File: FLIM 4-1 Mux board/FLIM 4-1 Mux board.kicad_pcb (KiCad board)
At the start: 4 copper layers, 74.5 x 100 mm, 59 parts, among them J2 RJ45_Shielded, J3 Conn_Coaxial, J4 Conn_Coaxial, J5 Conn_Coaxial, J6 Conn_Coaxial, J7 Conn_Coaxial, U1 ADM7150ARDZ-5.0, U2 74AHCT74D_118, U3 74AHCT74D_118, U4 SPDT RF switch, U5 SPDT RF switch, U6 SPDT RF switch

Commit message: Finished working draft of PCB - passes DRC
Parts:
- added J1: Barrel_Jack, Custom:CONN4_00165_TEN, F.Cu at (64.6, 41.7)
- moved J2 240.7 mm to (132.1, 50.9), turned to 90 degrees
- moved D4 218.6 mm to (117.0, 50.0)
- moved U3 213.5 mm to (108.0, 71.3)
- moved JP1 213.1 mm to (135.1, 62.6), turned to 90 degrees
- moved C18 209.0 mm to (133.3, 62.6), turned to -90 degrees
- moved C13 206.8 mm to (112.8, 67.0), turned to -90 degrees
- moved U2 206.3 mm to (92.0, 71.3)
- moved R1 199.0 mm to (95.7, 46.5)
- moved C9 197.8 mm to (103.6, 57.6), turned to -90 degrees
- moved C14 194.9 mm to (116.0, 56.4)
- moved C6 194.3 mm to (105.9, 46.0)
- moved C3 193.3 mm to (98.5, 47.5), turned to -90 degrees
- moved C15 192.8 mm to (113.9, 58.2), turned to -90 degrees
- moved C16 191.3 mm to (112.3, 58.2), turned to -90 degrees
- moved C12 190.5 mm to (96.8, 67.1), turned to -90 degrees
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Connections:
- D4 pad 1: /D1* -> /SH
- D4 pad 3: /SH -> /D1*
- D4 pad 4: /CLK* -> /D2*
- D4 pad 6: /D2* -> /CLK*
- RN1 pad 1: /CLK* -> /D1*
- RN1 pad 2: /D3* -> /D2*
- RN1 pad 3: /D2* -> /D3*
- RN1 pad 4: /D1* -> /CLK*
- RN1 pad 5: /D1 -> /CLK
- RN1 pad 6: /D2 -> /D3
- RN1 pad 7: /D3 -> /D2
- RN1 pad 8: /CLK -> /D1
- U2 pad 12: /D2 -> /D3
- U2 pad 2: /D1 -> /D2
- U2 pad 5: /A1 -> /A2
- U2 pad 6: /B1 -> /B2
- U2 pad 8: /B2 -> /B3
- U2 pad 9: /A2 -> /A3
- U3 pad 2: /D3 -> /D1
- U3 pad 5: /A3 -> /A1
- U3 pad 6: /B3 -> /B1
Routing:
- net GND: track 0.00 -> 309.3 mm, vias 0 -> 1602
- net +5VA: track 0.00 -> 85.4 mm, vias 0 -> 5
- net /CLK: track 0.00 -> 78.2 mm, vias 0 -> 8
- net /A2: track 0.00 -> 65.7 mm, vias 0 -> 2
- net /B3: track 0.00 -> 62.1 mm, vias 0 -> 2
- net /B2: track 0.00 -> 62.1 mm, vias 0 -> 2
- net /A3: track 0.00 -> 60.4 mm, vias 0 -> 2
- net /A1: track 0.00 -> 52.7 mm, vias 0 -> 2
- net /SH: track 0.00 -> 52.2 mm
- net /B1: track 0.00 -> 48.9 mm, vias 0 -> 2
- net /D2: track 0.00 -> 39.5 mm, vias 0 -> 3
- net /CLK*: track 0.00 -> 29.8 mm, vias 0 -> 4
- net /D1: track 0.00 -> 29.7 mm, vias 0 -> 3
- net /D3: track 0.00 -> 29.7 mm, vias 0 -> 3
- net /D3*: track 0.00 -> 26.3 mm, vias 0 -> 4
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- added copper zone on F.Cu, net +12VA
- added copper zone on F.Cu, net +5VA
- added copper zone on B.Cu, net GND
- added copper zone on In1.Cu, net GND
- added copper zone on In2.Cu, net GND
- added copper zone on F.Cu, net GNDPWR

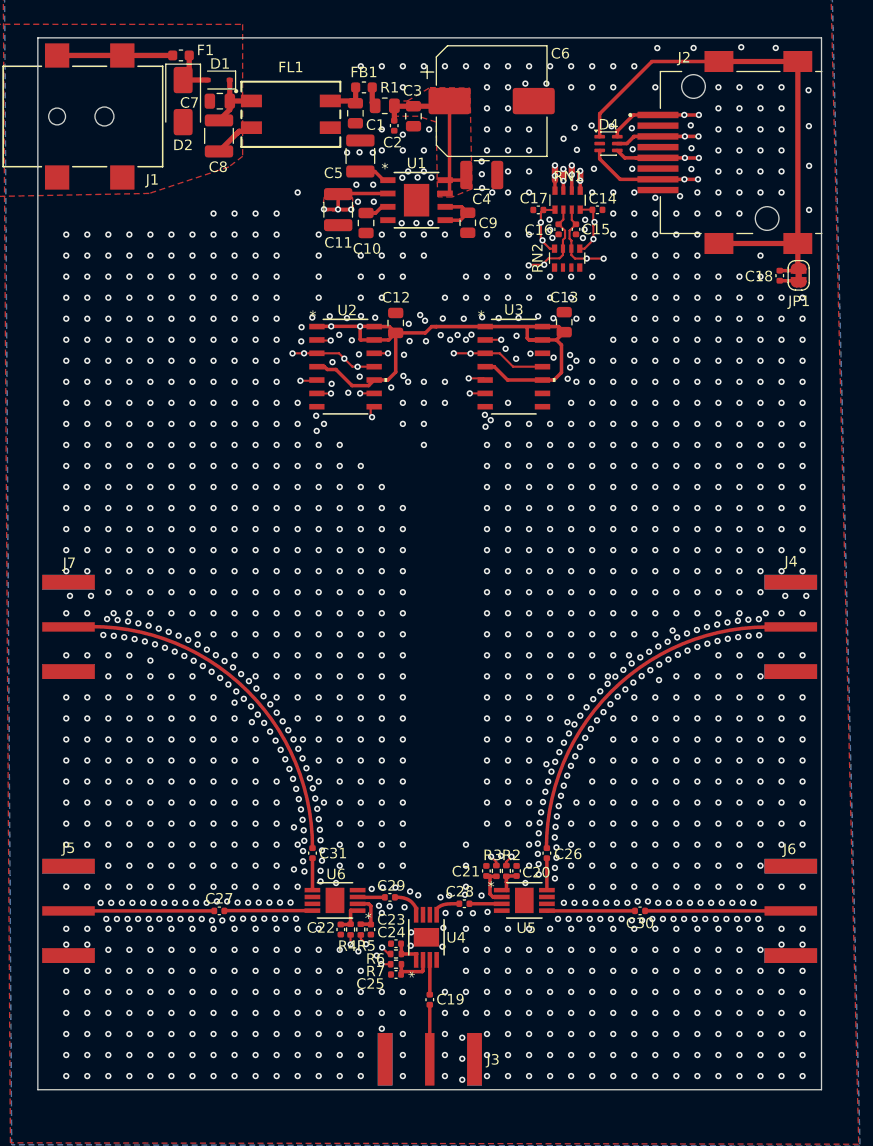
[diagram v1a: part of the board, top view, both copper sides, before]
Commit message: Backup copy of just guard vias, not ground stitching
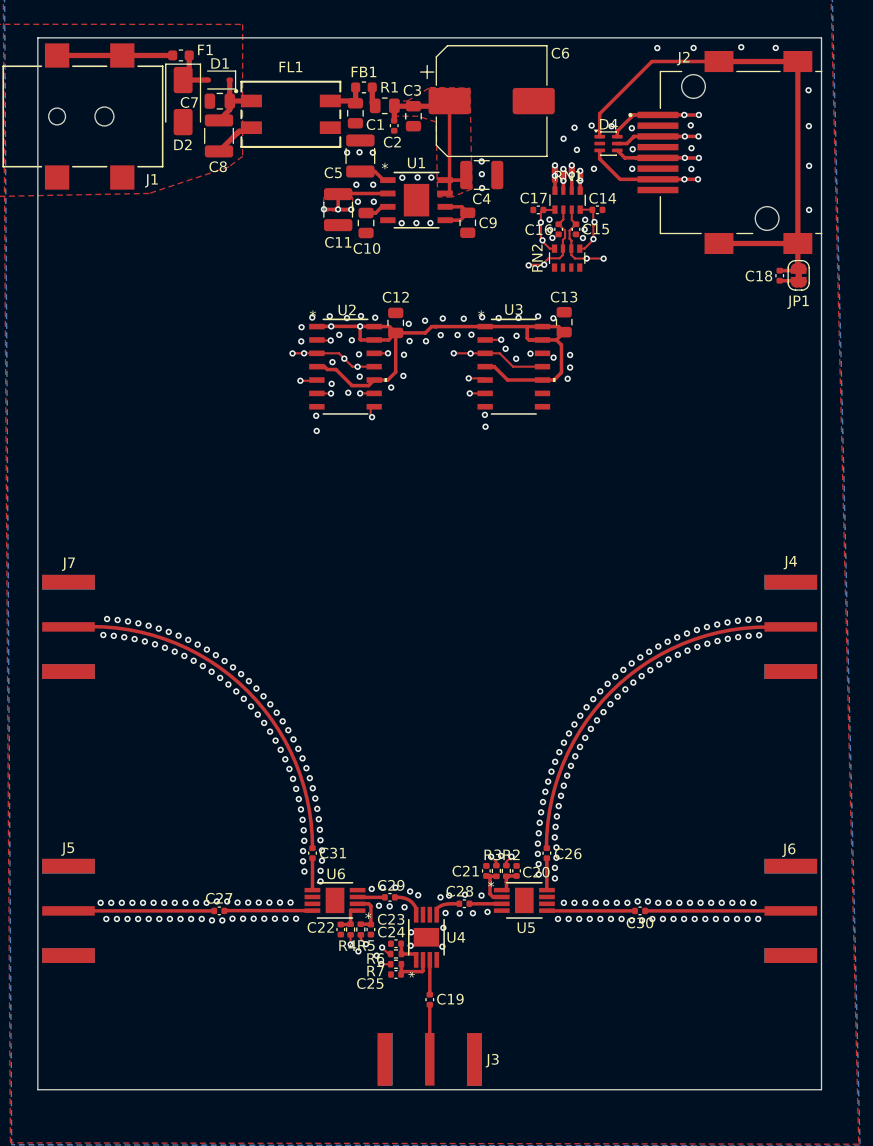
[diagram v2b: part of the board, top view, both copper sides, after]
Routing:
- net GND: vias 1602 -> 328

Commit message: Working draft with grnound stitching
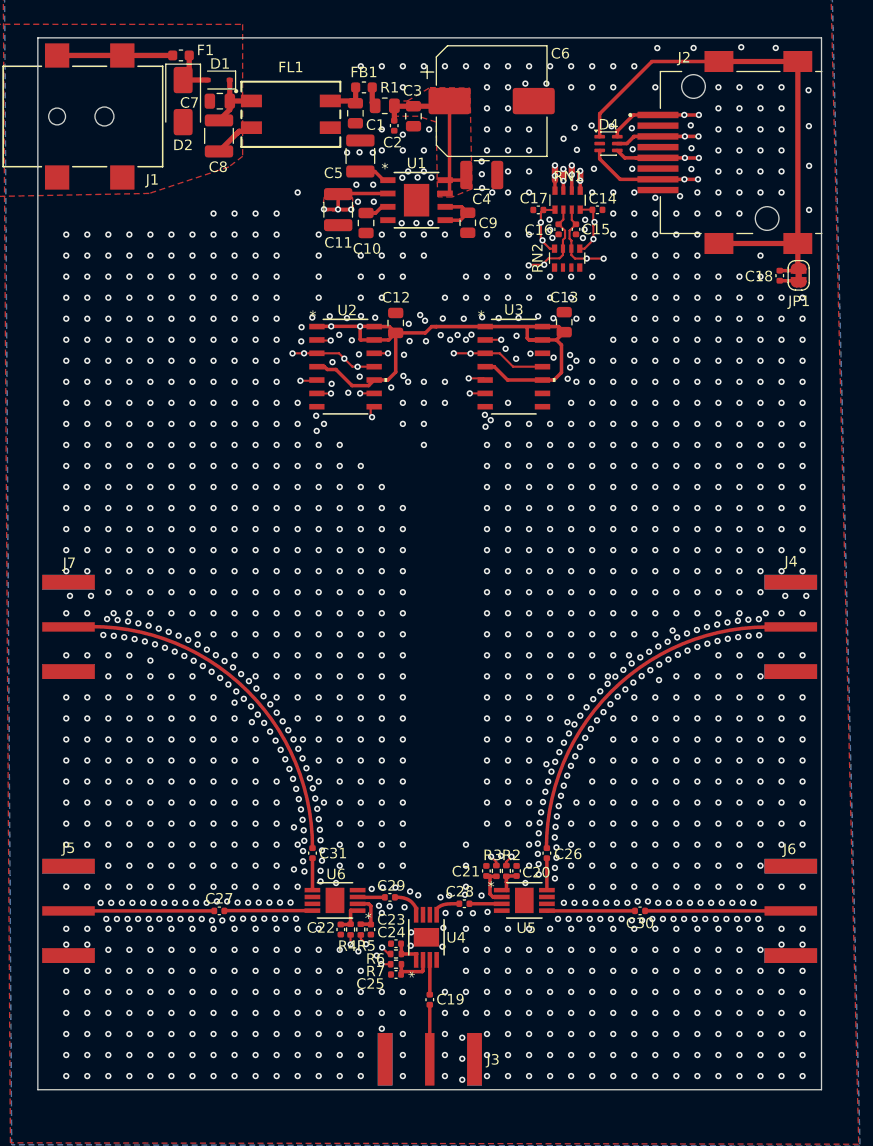
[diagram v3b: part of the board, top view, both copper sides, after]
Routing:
- net GND: vias 328 -> 1602

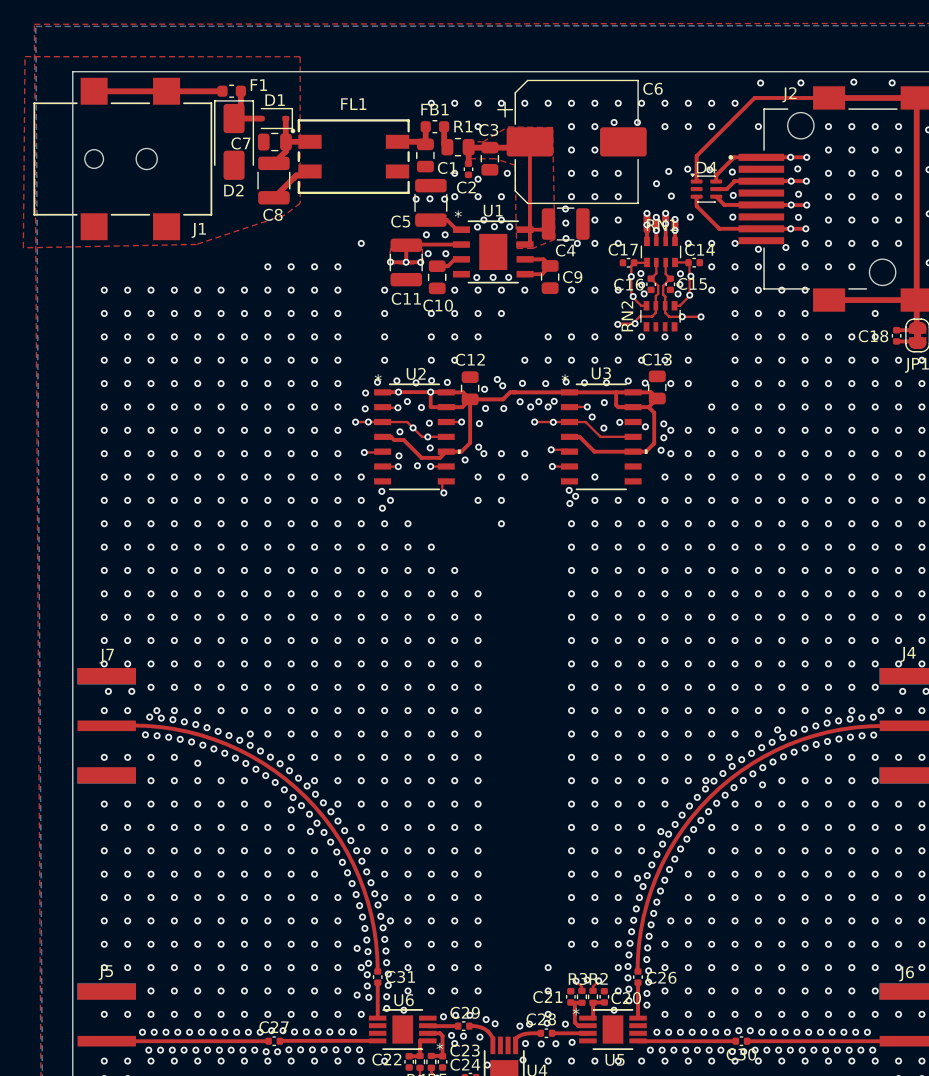
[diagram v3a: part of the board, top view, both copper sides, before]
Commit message: Better grounding and DC jack separation - SMA connectors need to be recessed
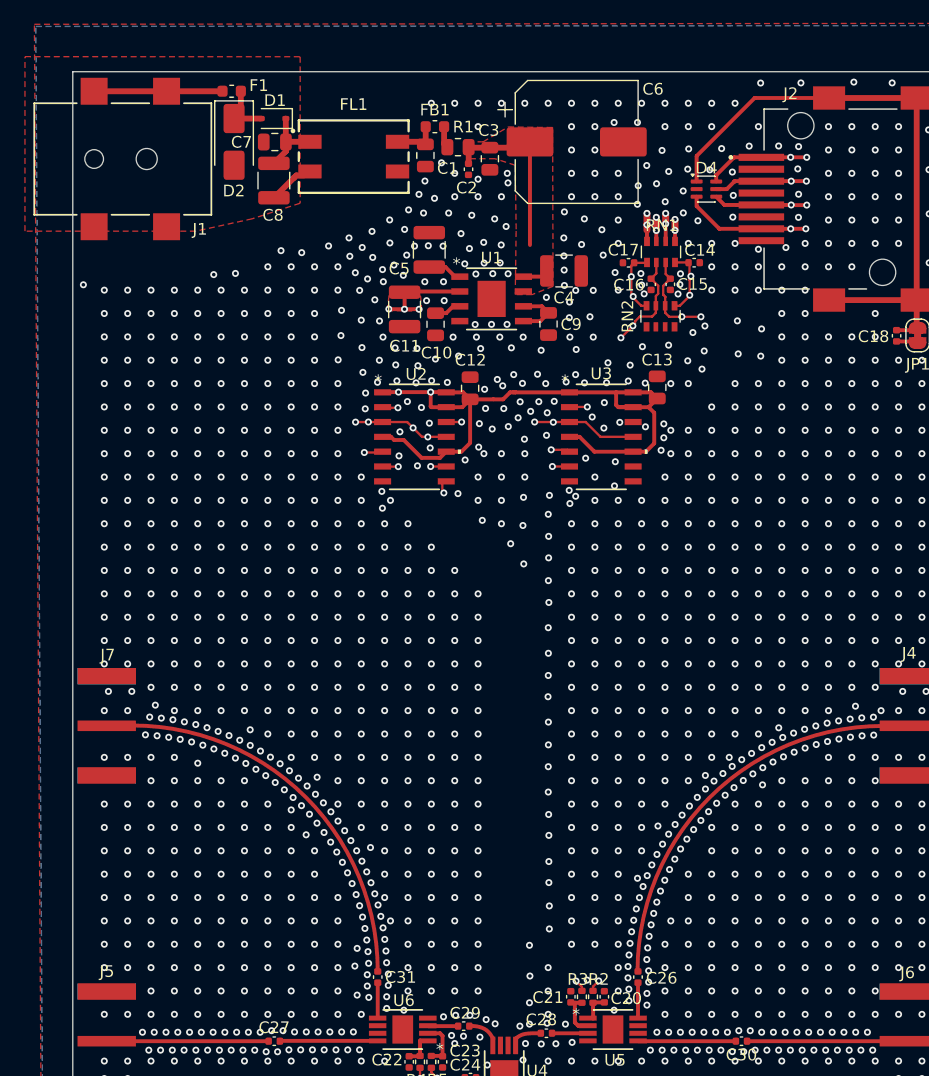
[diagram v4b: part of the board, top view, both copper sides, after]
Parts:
- moved C11 4.02 mm to (91.2, 60.4)
- moved C4 4.02 mm to (104.8, 57.1)
- moved C5 4.02 mm to (93.3, 55.2)
- moved C9 4.02 mm to (103.5, 61.6)
- moved U1 4.02 mm to (98.6, 59.5)
- moved C10 4.02 mm to (93.8, 61.6)
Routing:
- net +5VA: track 85.4 -> 81.5 mm
- net GND: track 309.3 -> 313.2 mm, vias 1602 -> 1696
- net /CLK: track 78.2 -> 74.5 mm

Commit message: Untested Impedance matching taper on SMA pins
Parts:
- added SYM1: Logo_Open_Hardware_Small, Symbol:OSHW-Logo_5.7x6mm_SilkScreen, F.Cu at (119.0, 82.8)
- added SYM2: Logo_Open_Hardware_Small, Custom:CC-BY-SA Symbol, F.Cu at (127.0, 81.9)
- moved J4 1.28 mm to (133.1, 96.0)
- moved J5 1.28 mm to (66.9, 123.0)
- moved J6 1.28 mm to (133.1, 123.0)
- moved J7 1.28 mm to (66.9, 96.0)
- moved C31 0.56 mm to (89.4, 117.5)
- moved C26 0.56 mm to (110.6, 117.5)
- moved J3 0.35 mm to (100.0, 137.5)
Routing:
- net GND: track 313.2 -> 331.1 mm, vias 1696 -> 1939
- net +5VA: track 81.5 -> 80.2 mm, vias 5 -> 6
- added copper zone on In2.Cu, net +5VA
- added copper zone on F.Cu, net Net-(J3-In)
- added copper zone on F.Cu, net Net-(J4-In)
- added copper zone on F.Cu, net Net-(J5-In)
- added copper zone on F.Cu, net Net-(J6-In)
- added copper zone on F.Cu, net Net-(J7-In)
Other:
- outline, holes or cut-outs redrawn
- board text added: "4:1 RF Mux - 400 kHz to 3 GHz"
- board text added: "COM"
- board text added: "Ch #1"
- board text added: "Ch #2"
- board text added: "Ch #3"
- board text added: "Ch #4"
- board text added: "Designed by: Benjamin E. Smith Funded by: RRID:SCR_017852 https://github.com/Llamero/FLIM_Sync_4-1_Mux"

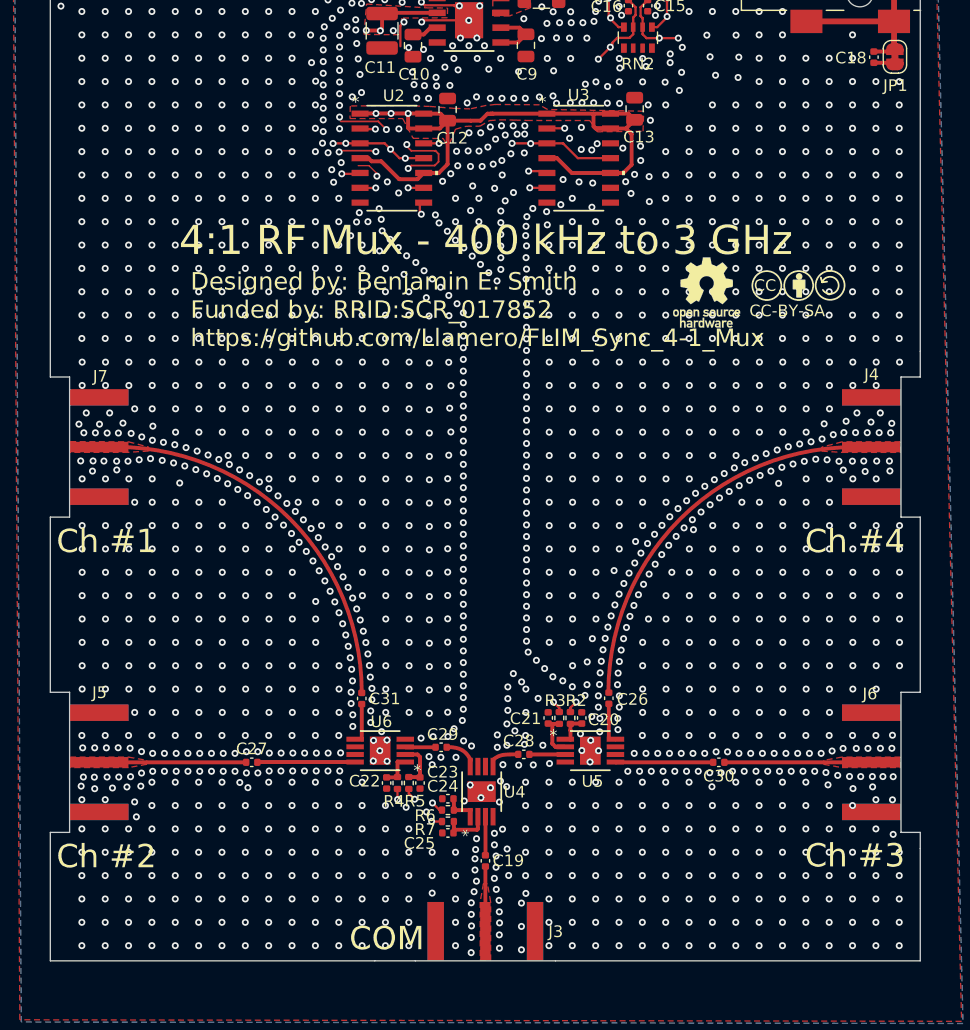
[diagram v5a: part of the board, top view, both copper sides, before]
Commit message: Shorten SMA pins to reduce impedance mismatch at 4GHz, add standoffs and enclosure
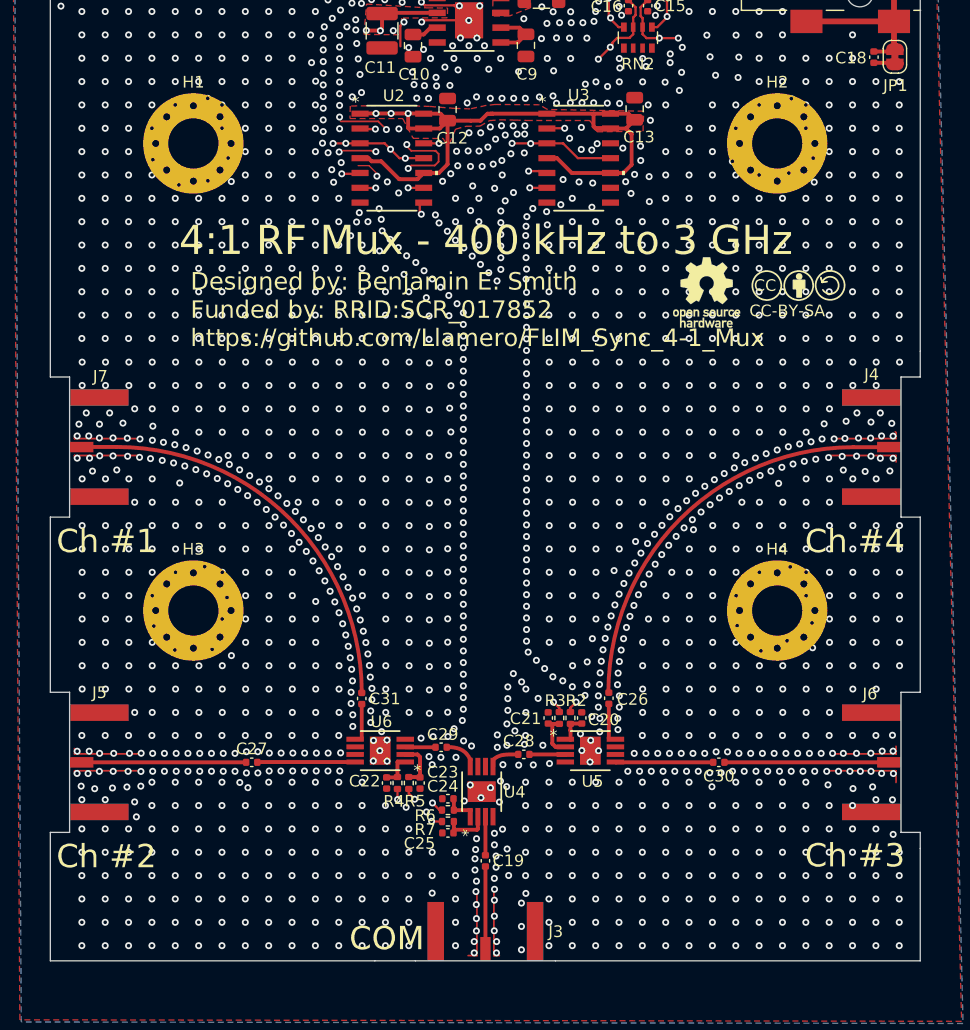
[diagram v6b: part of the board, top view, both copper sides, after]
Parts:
- added H1: ~, Custom:MountingHole_4.3mm_M4_Pad_Via, F.Cu at (75.0, 70.0)
- added H2: ~, Custom:MountingHole_4.3mm_M4_Pad_Via, F.Cu at (125.0, 70.0)
- added H3: ~, Custom:MountingHole_4.3mm_M4_Pad_Via, F.Cu at (75.0, 110.0)
- added H4: ~, Custom:MountingHole_4.3mm_M4_Pad_Via, F.Cu at (125.0, 110.0)
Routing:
- net GND: track 331.1 -> 392.7 mm, vias 1939 -> 1923
- net Net-(J4-In): track 32.1 -> 35.2 mm
- net Net-(J7-In): track 32.1 -> 35.1 mm
- net Net-(J3-In): track 5.19 -> 7.04 mm
- removed copper zone on F.Cu, net Net-(J3-In)
- removed copper zone on F.Cu, net Net-(J4-In)
- removed copper zone on F.Cu, net Net-(J5-In)
- removed copper zone on F.Cu, net Net-(J6-In)
- removed copper zone on F.Cu, net Net-(J7-In)
